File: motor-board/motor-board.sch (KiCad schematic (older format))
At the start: 12 parts, among them J1 Motor Driver IN, J2 Motor Driver OUT, J3 Regulator, J4 Ribbon Connector, J5 Battery, J6 Cape Power, J7 Right Motor JST, J8 Left Motor JST

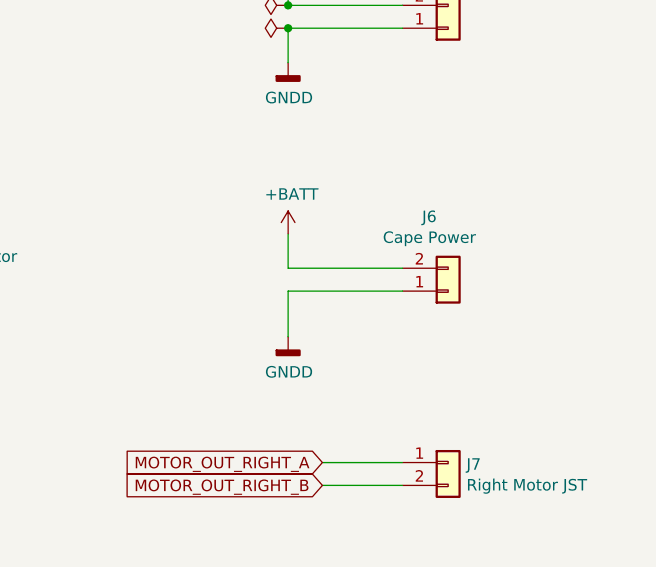
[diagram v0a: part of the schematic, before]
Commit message: Updated b2b power connector to 4-pin
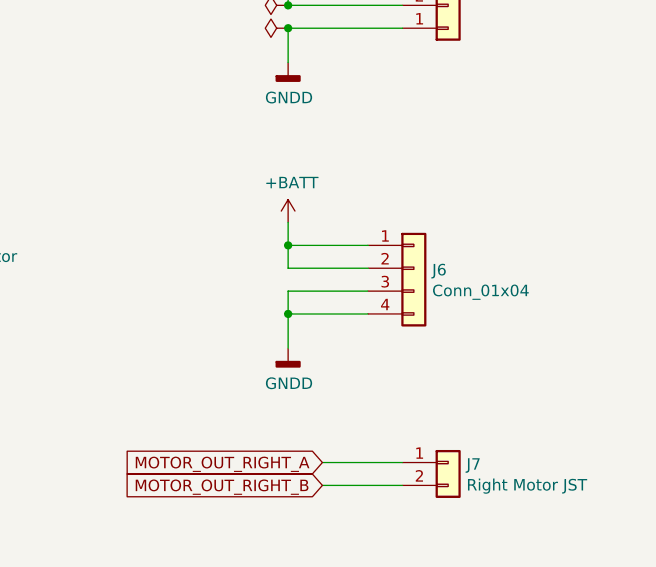
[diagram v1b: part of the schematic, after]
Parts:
- removed J6: Cape Power, Connector_Molex:Molex_KK-254_AE-6410-02A_1x02_P2.54mm_Vertical, symbol Connector_Generic:Conn_01x02
- added J6: Conn_01x04, Connector_Molex:Molex_KK-254_AE-6410-04A_1x04_P2.54mm_Vertical, symbol Connector_Generic:Conn_01x04
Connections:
- net +BATT: now also J6.1 (Pin_1), J6.2 (Pin_2)
- net GNDD: now also J6.3 (Pin_3), J6.4 (Pin_4)
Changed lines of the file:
@@
 L power:+BATT #PWR010
 U 1 1 5FE78920
-P 9000 2650
-F 0 "#PWR010" H 9000 2500 50  0001 C CNN
-F 1 "+BATT" H 9015 2823 50  0000 C CNN
-F 2 "" H 9000 2650 50  0001 C CNN
-F 3 "" H 9000 2650 50  0001 C CNN
-	1    9000 2650
-	1    0    0    -1
-$EndComp
-Wire Wire Line
-	9000 2650 9000 2800
-Wire Wire Line
-	9000 2900 9000 3100
+P 9000 2600
+F 0 "#PWR010" H 9000 2450 50  0001 C CNN
+F 1 "+BATT" H 9015 2773 50  0000 C CNN
+F 2 "" H 9000 2600 50  0001 C CNN
+F 3 "" H 9000 2600 50  0001 C CNN
+	1    9000 2600
+	1    0    0    -1
+$EndComp
 $Comp
 L Connector_Generic:Conn_01x02 J7
@@
 L power:GNDD #PWR0109
 U 1 1 5FE931DC
-P 9000 3100
-F 0 "#PWR0109" H 9000 2850 50  0001 C CNN
-F 1 "GNDD" H 9004 2945 50  0000 C CNN
-F 2 "" H 9000 3100 50  0001 C CNN
-F 3 "" H 9000 3100 50  0001 C CNN
-	1    9000 3100
+P 9000 3150
+F 0 "#PWR0109" H 9000 2900 50  0001 C CNN
+F 1 "GNDD" H 9004 2995 50  0000 C CNN
+F 2 "" H 9000 3150 50  0001 C CNN
+F 3 "" H 9000 3150 50  0001 C CNN
+	1    9000 3150
 	1    0    0    -1
 $EndComp
@@
 Wire Wire Line
 	9500 3650 9150 3650
-$Comp
-L Connector_Generic:Conn_01x02 J6
-U 1 1 5FE764C8
-P 9700 2900
-F 0 "J6" H 9618 2575 50  0000 C CNN
-F 1 "Cape Power" H 9618 2666 50  0000 C CNN
-F 2 "Connector_Molex:Molex_KK-254_AE-6410-02A_1x02_P2.54mm_Vertical" H 9700 2900 50  0001 C CNN
-F 3 "~" H 9700 2900 50  0001 C CNN
-	1    9700 2900
-	1    0    0    1
-$EndComp
-Wire Wire Line
-	9000 2800 9500 2800
-Wire Wire Line
-	9000 2900 9500 2900
 Connection ~ 9000 1650
 Connection ~ 9000 1750
@@
 Wire Wire Line
 	2900 1500 2450 1500
+$Comp
+L Connector_Generic:Conn_01x04 J6
+U 1 1 6017429D
+P 9550 2800
+F 0 "J6" H 9630 2792 50  0000 L CNN
+F 1 "Conn_01x04" H 9630 2701 50  0000 L CNN
+F 2 "Connector_Molex:Molex_KK-254_AE-6410-04A_1x04_P2.54mm_Vertical" H 9550 2800 50  0001 C CNN
+F 3 "~" H 9550 2800 50  0001 C CNN
+	1    9550 2800
+	1    0    0    -1
+$EndComp
+Wire Wire Line
+	9000 2600 9000 2700
+Wire Wire Line
+	9000 2700 9350 2700
+Wire Wire Line
+	9350 2800 9000 2800
+Wire Wire Line
+	9000 2800 9000 2700
+Connection ~ 9000 2700
+Wire Wire Line
+	9350 3000 9000 3000
+Wire Wire Line
+	9000 3000 9000 3150
+Wire Wire Line
+	9350 2900 9000 2900
+Wire Wire Line
+	9000 2900 9000 3000
+Connection ~ 9000 3000
 $EndSCHEMATC

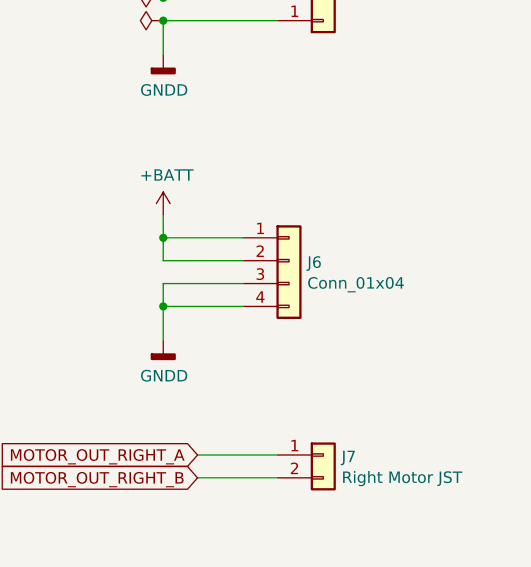
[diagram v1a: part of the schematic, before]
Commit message: Fixed b2b power header names, improved motor board layout
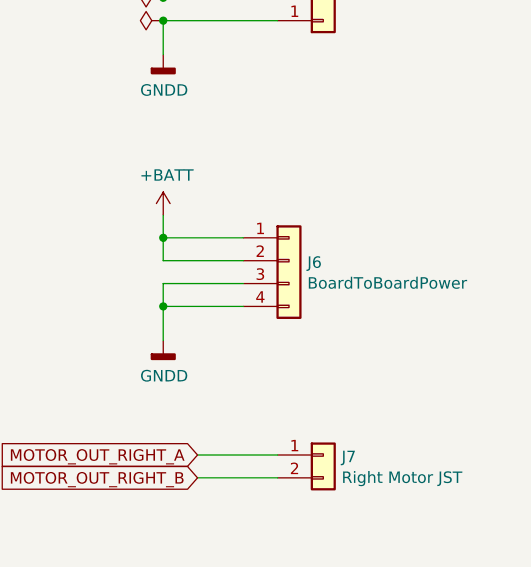
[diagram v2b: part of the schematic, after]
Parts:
- J6: value Conn_01x04 -> BoardToBoardPower
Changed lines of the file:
@@
 P 9550 2800
 F 0 "J6" H 9630 2792 50  0000 L CNN
-F 1 "Conn_01x04" H 9630 2701 50  0000 L CNN
+F 1 "BoardToBoardPower" H 9630 2701 50  0000 L CNN
 F 2 "Connector_Molex:Molex_KK-254_AE-6410-04A_1x04_P2.54mm_Vertical" H 9550 2800 50  0001 C CNN
 F 3 "~" H 9550 2800 50  0001 C CNN

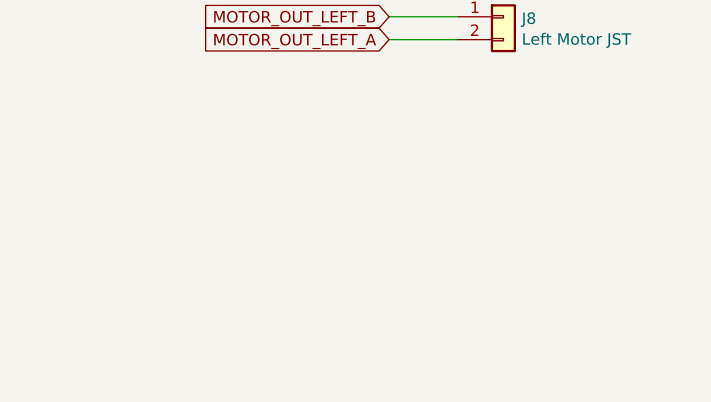
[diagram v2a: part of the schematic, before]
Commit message: Added power LED to motor board
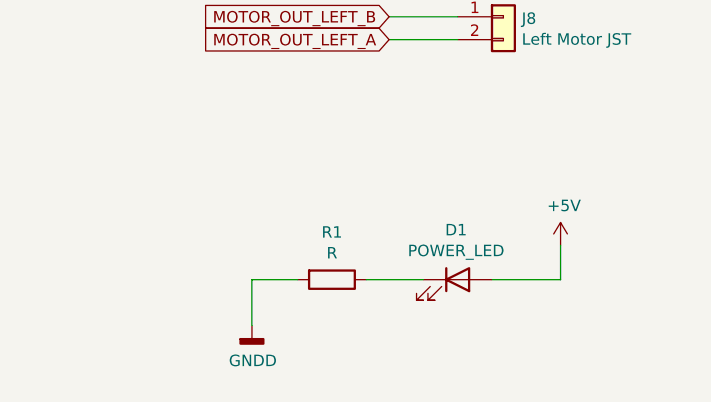
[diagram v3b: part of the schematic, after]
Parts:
- added D1: POWER_LED, LED_SMD:LED_0805_2012Metric_Pad1.15x1.40mm_HandSolder, symbol Device:LED
- added R1: R, Resistor_SMD:R_0805_2012Metric_Pad1.20x1.40mm_HandSolder, symbol Device:R
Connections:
- net +5V: now also D1.2 (A)
- net GNDD: now also R1.2
- new net: D1.1 (K), R1.1
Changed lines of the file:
@@
 	9000 2900 9000 3000
 Connection ~ 9000 3000
+$Comp
+L Device:LED D1
+U 1 1 6034D106
+P 9500 5450
+F 0 "D1" H 9493 5667 50  0000 C CNN
+F 1 "POWER_LED" H 9493 5576 50  0000 C CNN
+F 2 "LED_SMD:LED_0805_2012Metric_Pad1.15x1.40mm_HandSolder" H 9500 5450 50  0001 C CNN
+F 3 "~" H 9500 5450 50  0001 C CNN
+	1    9500 5450
+	1    0    0    -1
+$EndComp
+$Comp
+L Device:R R1
+U 1 1 6034E90E
+P 8950 5450
+F 0 "R1" V 8743 5450 50  0000 C CNN
+F 1 "R" V 8834 5450 50  0000 C CNN
+F 2 "Resistor_SMD:R_0805_2012Metric_Pad1.20x1.40mm_HandSolder" V 8880 5450 50  0001 C CNN
+F 3 "~" H 8950 5450 50  0001 C CNN
+	1    8950 5450
+	0    1    1    0
+$EndComp
+$Comp
+L power:GNDD #PWR01
+U 1 1 6034F7E0
+P 8600 5650
+F 0 "#PWR01" H 8600 5400 50  0001 C CNN
+F 1 "GNDD" H 8604 5495 50  0000 C CNN
+F 2 "" H 8600 5650 50  0001 C CNN
+F 3 "" H 8600 5650 50  0001 C CNN
+	1    8600 5650
+	1    0    0    -1
+$EndComp
+$Comp
+L power:+5V #PWR02
+U 1 1 6034FC87
+P 9950 5300
+F 0 "#PWR02" H 9950 5150 50  0001 C CNN
+F 1 "+5V" H 9965 5473 50  0000 C CNN
+F 2 "" H 9950 5300 50  0001 C CNN
+F 3 "" H 9950 5300 50  0001 C CNN
+	1    9950 5300
+	1    0    0    -1
+$EndComp
+Wire Wire Line
+	8800 5450 8600 5450
+Wire Wire Line
+	8600 5450 8600 5650
+Wire Wire Line
+	9100 5450 9350 5450
+Wire Wire Line
+	9650 5450 9950 5450
+Wire Wire Line
+	9950 5450 9950 5300
 $EndSCHEMATC
